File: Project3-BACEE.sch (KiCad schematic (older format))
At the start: 13 parts, among them U1 24LC1025, U2 24LC1025, U3 DS1337_CSP, U4 ATMEGA328P-AU, Y1 Crystal 32MHz, Y2 Crystal 16MHz

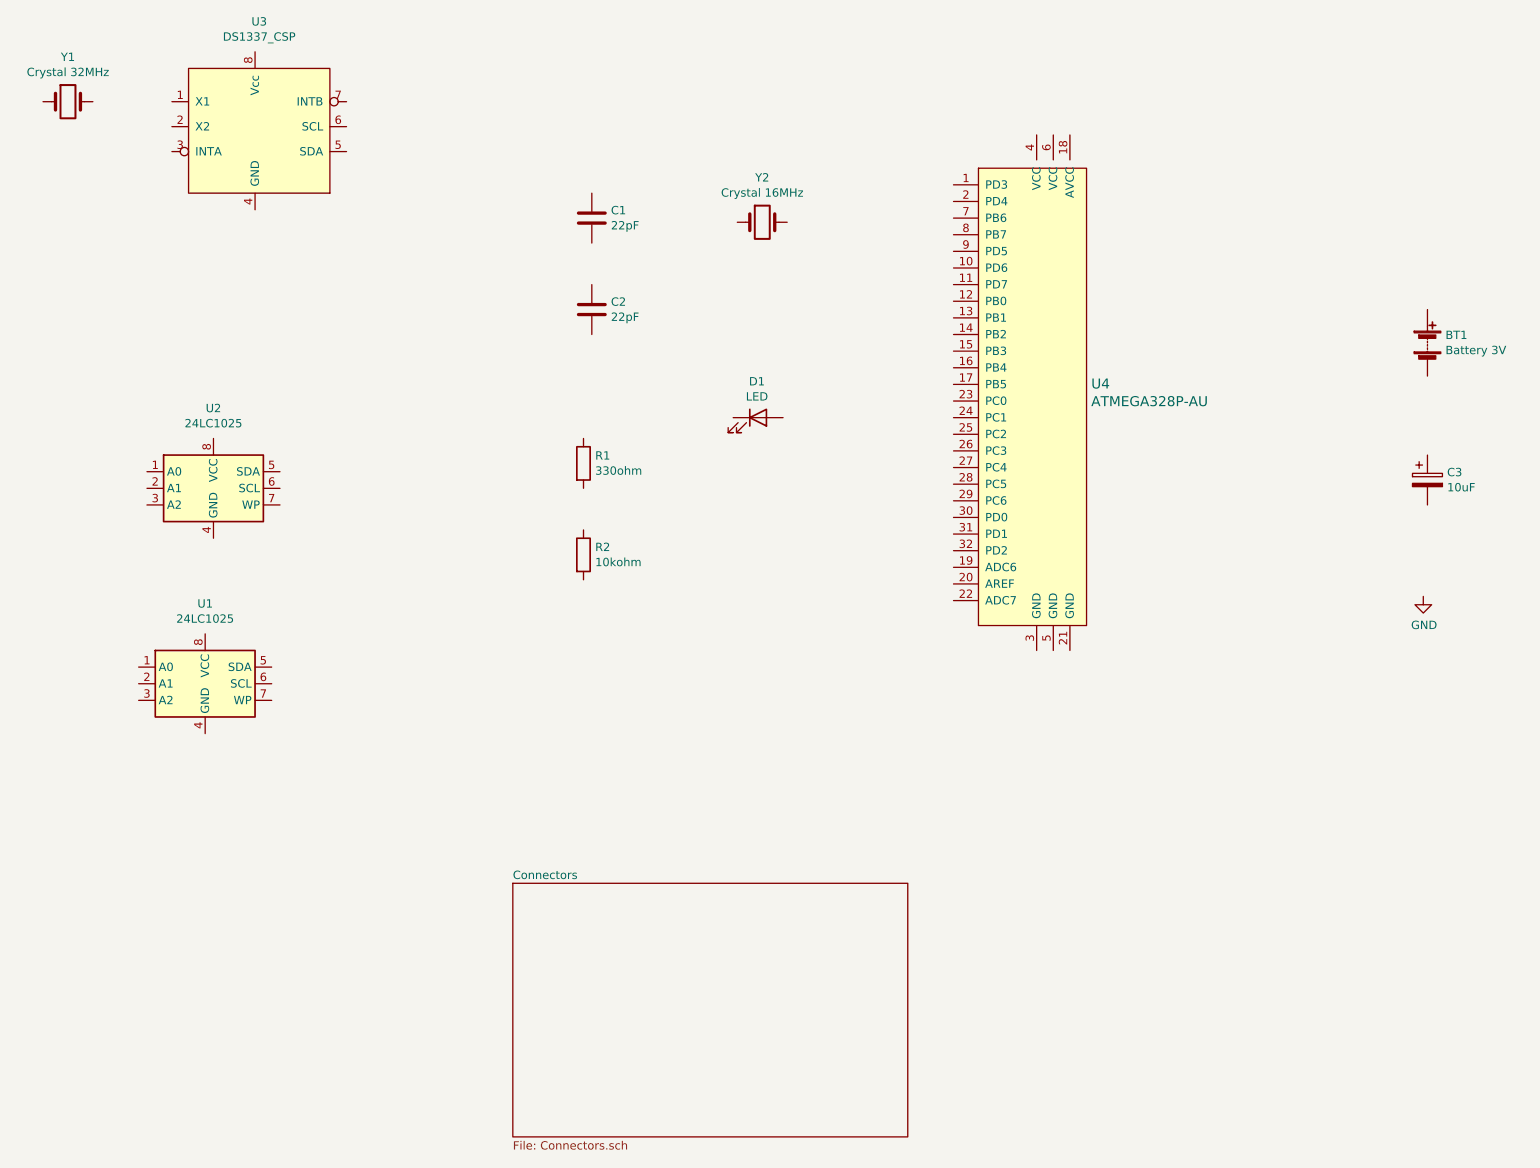
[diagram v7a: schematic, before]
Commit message: wiring on connectors sheet
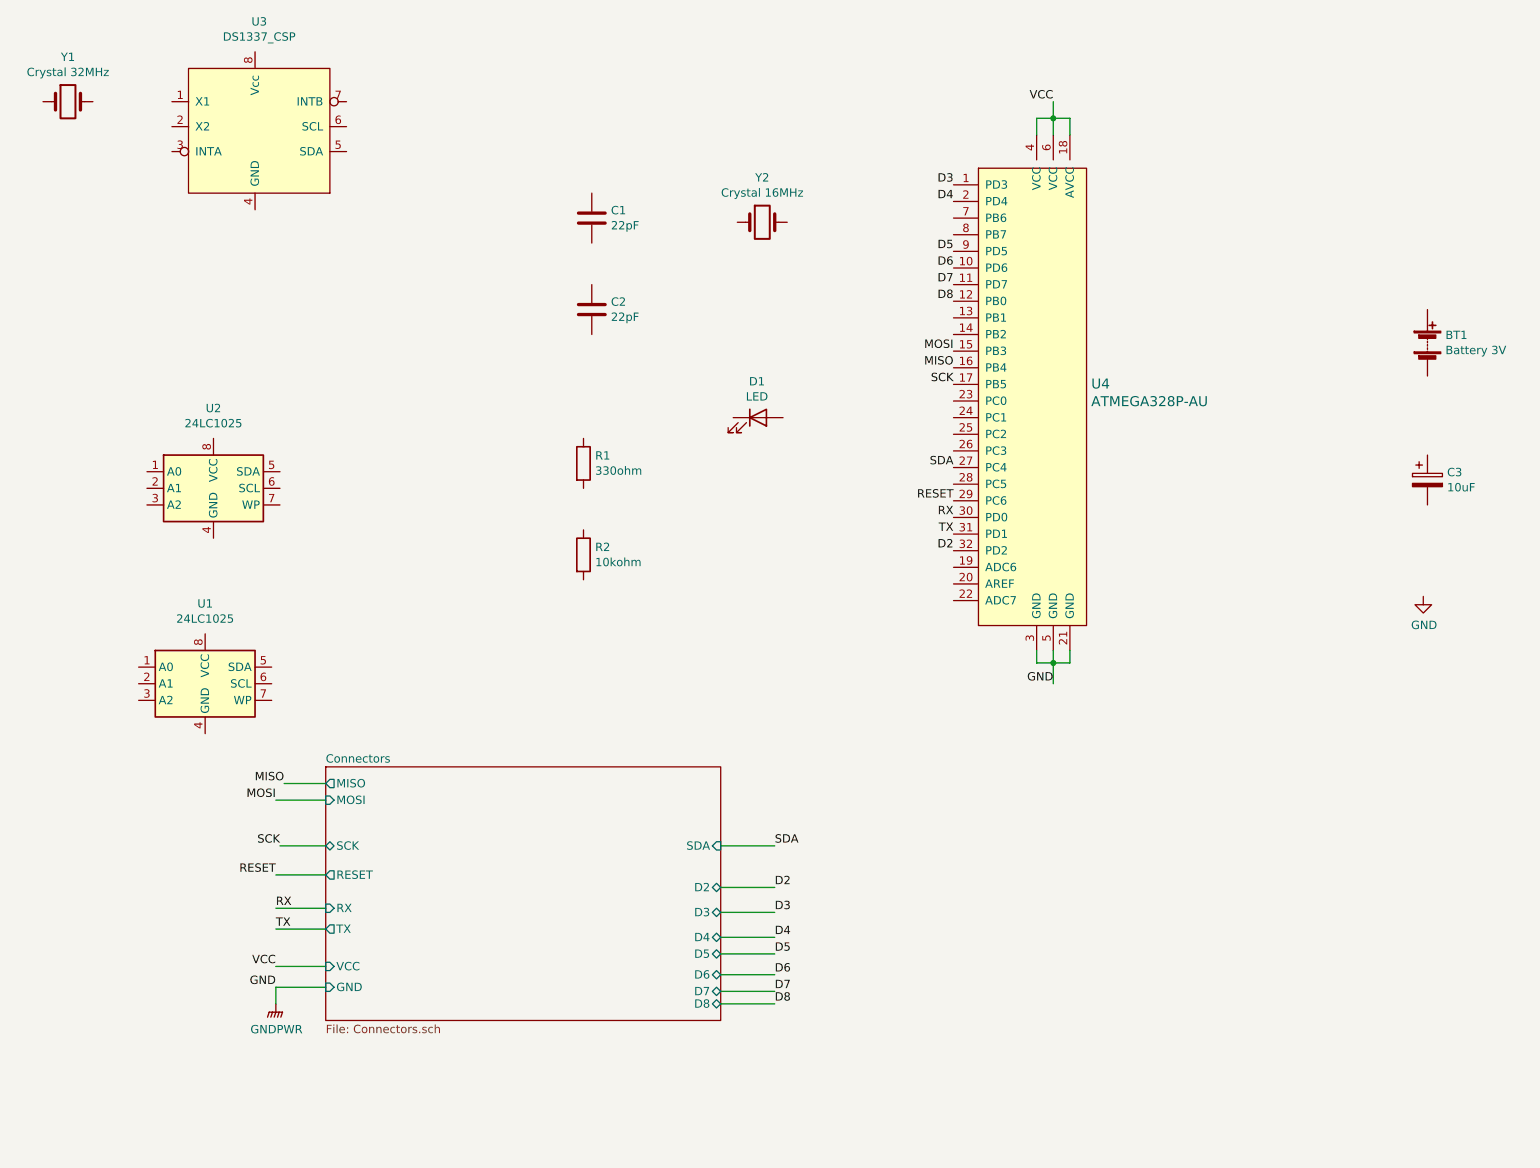
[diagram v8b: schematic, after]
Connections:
- net GND: now also U4.21 (GND), U4.3 (GND), U4.5 (GND)
- net D3: now reaches U4.1 (PD3)
- net D6: now reaches U4.10 (PD6)
- net D7: now reaches U4.11 (PD7)
- net D8: now reaches U4.12 (PB0)
- net MOSI: now reaches U4.15 (PB3)
- net MISO: now reaches U4.16 (PB4)
- net SCK: now reaches U4.17 (PB5)
- net VCC: now reaches U4.18 (AVCC)
- net VCC: now also U4.4 (VCC), U4.6 (VCC)
- net D4: now reaches U4.2 (PD4)
- net SDA: now reaches U4.27 (PC4)
- net RESET: now reaches U4.29 (PC6)
- net RX: now reaches U4.30 (PD0)
- net TX: now reaches U4.31 (PD1)
- net D2: now reaches U4.32 (PD2)
- net D5: now reaches U4.9 (PD5)
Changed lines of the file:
@@
 	1    0    0    -1
 $EndComp
-$Sheet
-S 4450 6125 2375 1525
-U 61A1FED7
-F0 "Connectors" 50
-F1 "Connectors.sch" 50
-$EndSheet
 $Comp
 L dk_Embedded-Microcontrollers:ATMEGA328P-AU U4
@@
 	1    0    0    -1
 $EndComp
+Text Label 7100 3025 2    50   ~ 0
+MISO
+Text Label 7100 2925 2    50   ~ 0
+MOSI
+Text Label 7100 3125 2    50   ~ 0
+SCK
+Text Label 7100 3825 2    50   ~ 0
+RESET
+Text Label 7700 1425 2    50   ~ 0
+VCC
+Wire Wire Line
+	7600 1625 7600 1525
+Wire Wire Line
+	7600 1525 7700 1525
+Wire Wire Line
+	7800 1525 7800 1625
+Wire Wire Line
+	7700 1525 7700 1625
+Connection ~ 7700 1525
+Wire Wire Line
+	7700 1525 7800 1525
+Wire Wire Line
+	7700 1525 7700 1425
+Text Label 7700 4925 2    50   ~ 0
+GND
+Wire Wire Line
+	7600 4725 7600 4800
+Wire Wire Line
+	7600 4800 7700 4800
+Wire Wire Line
+	7800 4800 7800 4725
+Wire Wire Line
+	7700 4725 7700 4800
+Connection ~ 7700 4800
+Wire Wire Line
+	7700 4800 7800 4800
+Wire Wire Line
+	7700 4925 7700 4800
+Wire Wire Line
+	3025 6850 3025 6750
+$Comp
+L power:GNDPWR #PWR?
+U 1 1 61A988D5
+P 3025 6850
+F 0 "#PWR?" H 3025 6650 50  0001 C CNN
+F 1 "GNDPWR" H 3029 6696 50  0000 C CNN
+F 2 "" H 3025 6800 50  0001 C CNN
+F 3 "" H 3025 6800 50  0001 C CNN
+	1    3025 6850
+	1    0    0    -1
+$EndComp
+Wire Wire Line
+	3025 6750 3325 6750
+Wire Wire Line
+	3025 5625 3325 5625
+Wire Wire Line
+	3025 6625 3325 6625
+Wire Wire Line
+	3025 6075 3325 6075
+Wire Wire Line
+	3050 5900 3325 5900
+Text Label 3025 6750 2    50   ~ 0
+GND
+Text Label 3025 5625 2    50   ~ 0
+MOSI
+Text Label 3025 6625 2    50   ~ 0
+VCC
+Text Label 3025 6075 2    50   ~ 0
+RESET
+Text Label 3050 5900 2    50   ~ 0
+SCK
+Wire Wire Line
+	3075 5525 3325 5525
+Text Label 3075 5525 2    50   ~ 0
+MISO
+$Sheet
+S 3325 5425 2375 1525
+U 61A1FED7
+F0 "Connectors" 50
+F1 "Connectors.sch" 50
+F2 "MISO" O L 3325 5525 50
+F3 "SCK" B L 3325 5900 50
+F4 "RESET" O L 3325 6075 50
+F5 "VCC" I L 3325 6625 50
+F6 "MOSI" I L 3325 5625 50
+F7 "GND" I L 3325 6750 50
+F8 "RX" I L 3325 6275 50
+F9 "TX" O L 3325 6400 50
+F10 "SDA" I R 5700 5900 50
+F11 "D2" B R 5700 6150 50
+F12 "D3" B R 5700 6300 50
+F13 "D4" B R 5700 6450 50
+F14 "D5" B R 5700 6550 50
+F15 "D6" B R 5700 6675 50
+F16 "D7" B R 5700 6775 50
+F17 "D8" B R 5700 6850 50
+$EndSheet
+Text Label 6025 5900 0    50   ~ 0
+SDA
+Text Label 6025 6150 0    50   ~ 0
+D2
+Text Label 6025 6300 0    50   ~ 0
+D3
+Text Label 6025 6450 0    50   ~ 0
+D4
+Text Label 6025 6550 0    50   ~ 0
+D5
+Text Label 6025 6675 0    50   ~ 0
+D6
+Text Label 6025 6775 0    50   ~ 0
+D7
+Text Label 6025 6850 0    50   ~ 0
+D8
+Text Label 3025 6275 0    50   ~ 0
+RX
+Text Label 3025 6400 0    50   ~ 0
+TX
+Wire Wire Line
+	6025 5900 5700 5900
+Wire Wire Line
+	5700 6150 6025 6150
+Wire Wire Line
+	5700 6300 6025 6300
+Wire Wire Line
+	5700 6450 6025 6450
+Wire Wire Line
+	5700 6550 6025 6550
+Wire Wire Line
+	5700 6675 6025 6675
+Wire Wire Line
+	5700 6775 6025 6775
+Wire Wire Line
+	5700 6850 6025 6850
+Wire Wire Line
+	3325 6400 3025 6400
+Wire Wire Line
+	3025 6275 3325 6275
+Text Label 7100 1925 2    50   ~ 0
+D3
+Text Label 7100 2025 2    50   ~ 0
+D4
+Text Label 7100 2325 2    50   ~ 0
+D5
+Text Label 7100 2425 2    50   ~ 0
+D6
+Text Label 7100 2525 2    50   ~ 0
+D7
+Text Label 7100 2625 2    50   ~ 0
+D8
+Text Label 7100 3625 2    50   ~ 0
+SDA
+Text Label 7100 3925 2    50   ~ 0
+RX
+Text Label 7100 4025 2    50   ~ 0
+TX
+Text Label 7100 4125 2    50   ~ 0
+D2
 $EndSCHEMATC
